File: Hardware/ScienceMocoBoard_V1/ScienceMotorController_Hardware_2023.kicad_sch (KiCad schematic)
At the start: 185 parts, among them J1 RJ45_LED_Shielded, J2 Conn_02x03_Counter_Clockwise, Q1 SI4156DY, Q10 SI4156DY, Q11 SI4156DY, Q12 SI4156DY, Q13 SI4156DY, Q14 SI4156DY, Q15 SI4156DY, Q16 SI4156DY, Q2 SI4156DY, Q3 SI4156DY, Q4 SI4156DY, Q5 SI4156DY, Q6 SI4156DY, Q7 SI4156DY, Q8 SI4156DY, Q9 SI4156DY, SW1 SW_Push, SW10 SW_Push, SW11 SW_DPDT_x2, SW2 SW_Push, SW3 SW_Push, SW4 SW_Push, SW5 SW_Push, SW6 SW_Push, SW7 SW_Push, SW8 SW_Push, SW9 SW_Push, U1 74LVC2G04, U10 IRS2005S, U11 Teensy4.1_DEV-16771, U12 74LVC2G04, U13 IRS2005S, U14 IRS2005S, U15 IRS2005S, U2 IRS2005S, U3 3V3 OKI, U4 TSR_1-2450, U5 74LVC2G04, U6 IRS2005S, U7 IRS2005S, U8 IRS2005S, U9 74LVC2G04

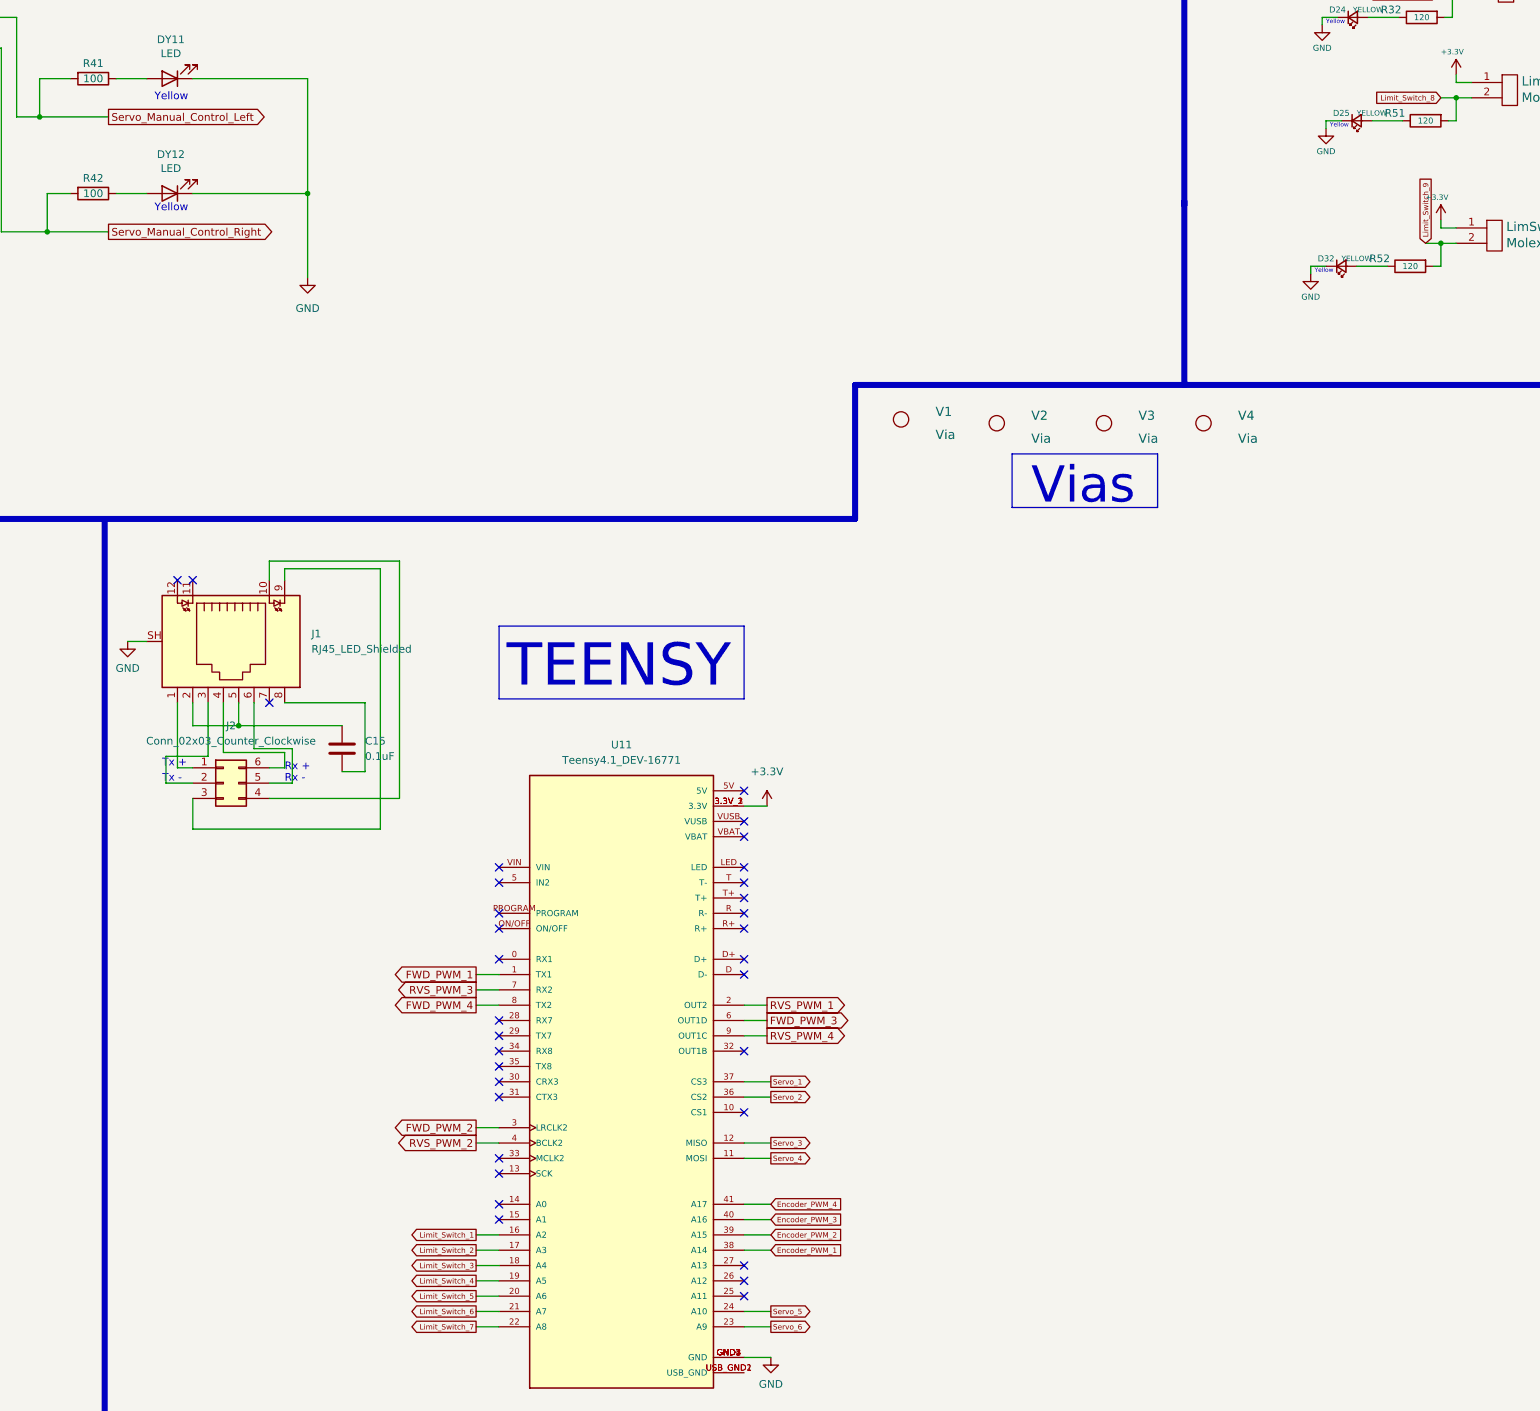
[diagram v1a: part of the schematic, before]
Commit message: H-Bridges organized and on board. PCB components sorted.
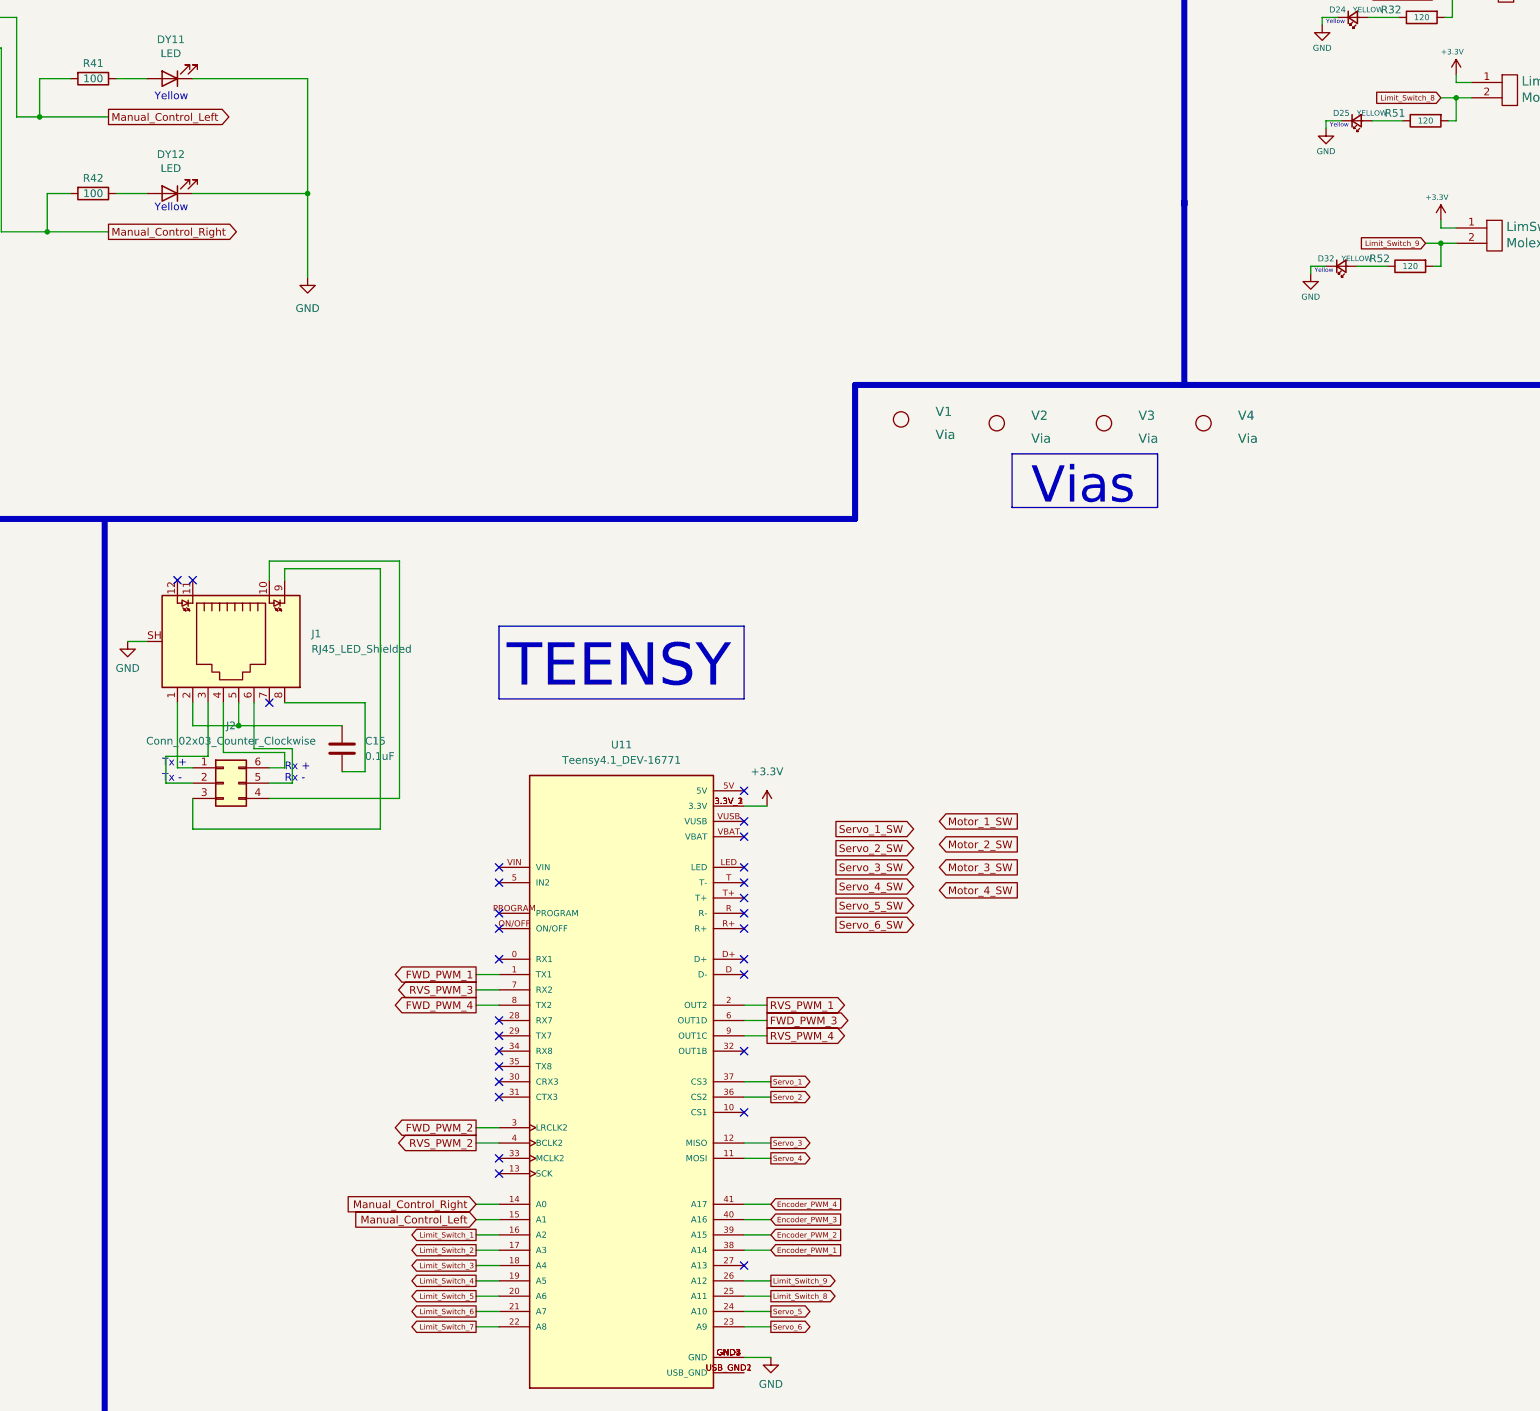
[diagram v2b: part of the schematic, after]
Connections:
- net Servo_Manual_Control_Left is gone; now on net Manual_Control_Left: R41.2, SW11.1 (A)
- net Servo_Manual_Control_Right is gone; now on net Manual_Control_Right: R42.2, SW11.3 (C)
- net Limit_Switch_8: now also U11.25 (A11)
- net Limit_Switch_9: now also U11.26 (A12)
- net Manual_Control_Right: now reaches U11.14 (A0)
- net Manual_Control_Left: now reaches U11.15 (A1)
- no-connect marks 33 -> 29
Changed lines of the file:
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@@
   (no_connect (at 422.275 319.405))
   (no_connect (at 422.275 349.885))
-  (no_connect (at 422.275 380.365))
-  (no_connect (at 422.275 377.825))
   (no_connect (at 422.275 375.285))
-  (no_connect (at 381.635 367.665))
   (no_connect (at 422.275 339.725))
   (no_connect (at 381.635 357.505))
@@
   (no_connect (at 381.635 316.865))
   (no_connect (at 381.635 319.405))
-  (no_connect (at 381.635 365.125))
   (wire (pts (xy 235.585 61.595) (xy 235.585 62.865))
     (stroke (width 0) (type default) (color 0 0 0 0))
@@
     (stroke (width 0) (type default) (color 0 0 0 0))
   )
+  (wire (pts (xy 377.825 367.665) (xy 381.635 367.665))
+    (stroke (width 0) (type default) (color 0 0 0 0))
+  )
   (wire (pts (xy 225.425 40.005) (xy 225.425 33.655))
     (stroke (width 0) (type default) (color 0 0 0 0))
@@
   )
   (wire (pts (xy 362.585 48.895) (xy 362.585 50.165))
+    (stroke (width 0) (type default) (color 0 0 0 0))
+  )
+  (wire (pts (xy 422.275 380.365) (xy 426.72 380.365))
     (stroke (width 0) (type default) (color 0 0 0 0))
   )
@@
     (stroke (width 0) (type default) (color 0 0 0 0))
   )
+  (wire (pts (xy 422.275 377.825) (xy 426.72 377.825))
+    (stroke (width 0) (type default) (color 0 0 0 0))
+  )
   (wire (pts (xy 224.79 229.87) (xy 228.6 229.87))
     (stroke (width 0) (type default) (color 0 0 0 0))
@@
   )
   (wire (pts (xy 387.985 100.965) (xy 387.985 94.615))
+    (stroke (width 0) (type default) (color 0 0 0 0))
+  )
+  (wire (pts (xy 377.825 365.125) (xy 381.635 365.125))
     (stroke (width 0) (type default) (color 0 0 0 0))
   )
@@
     )
   )
+  (global_label "Limit_Switch_8" (shape output) (at 426.72 380.365 0) (fields_autoplaced)
+    (effects (font (size 0.889 0.889)) (justify left))
+    (property "Intersheet References" "${INTERSHEET_REFS}" (id 0) (at 438.1458 380.4205 0)
+      (effects (font (size 0.889 0.889)) (justify left) hide)
+    )
+  )
   (global_label "RVS_PWM_1" (shape input) (at 264.795 40.005 0) (fields_autoplaced)
     (effects (font (size 1.27 1.27)) (justify left))
@@
     )
   )
+  (global_label "Manual_Control_Right" (shape input) (at 377.825 365.125 180) (fields_autoplaced)
+    (effects (font (size 1.27 1.27)) (justify right))
+    (property "Intersheet References" "${INTERSHEET_REFS}" (id 0) (at 354.9709 365.2044 0)
+      (effects (font (size 1.27 1.27)) (justify right) hide)
+    )
+  )
+  (global_label "Servo_2_SW" (shape output) (at 437.515 306.07 0) (fields_autoplaced)
+    (effects (font (size 1.27 1.27)) (justify left))
+    (property "Intersheet References" "${INTERSHEET_REFS}" (id 0) (at 450.9348 305.9906 0)
+      (effects (font (size 1.27 1.27)) (justify left) hide)
+    )
+  )
+  (global_label "Servo_3_SW" (shape output) (at 437.515 309.245 0) (fields_autoplaced)
+    (effects (font (size 1.27 1.27)) (justify left))
+    (property "Intersheet References" "${INTERSHEET_REFS}" (id 0) (at 450.9348 309.1656 0)
+      (effects (font (size 1.27 1.27)) (justify left) hide)
+    )
+  )
   (global_label "Motor_4_SW" (shape output) (at 233.68 219.71 0) (fields_autoplaced)
     (effects (font (size 1.27 1.27)) (justify left))
@@
     )
   )
-  (global_label "Limit_Switch_9" (shape input) (at 535.305 205.74 90) (fields_autoplaced)
-    (effects (font (size 0.889 0.889)) (justify left))
-    (property "Intersheet References" "${INTERSHEET_REFS}" (id 0) (at 535.3605 194.3142 90)
-      (effects (font (size 0.889 0.889)) (justify left) hide)
+  (global_label "Servo_5_SW" (shape output) (at 437.515 315.595 0) (fields_autoplaced)
+    (effects (font (size 1.27 1.27)) (justify left))
+    (property "Intersheet References" "${INTERSHEET_REFS}" (id 0) (at 450.9348 315.5156 0)
+      (effects (font (size 1.27 1.27)) (justify left) hide)
+    )
+  )
+  (global_label "Manual_Control_Left" (shape input) (at 377.825 367.665 180) (fields_autoplaced)
+    (effects (font (size 1.27 1.27)) (justify right))
+    (property "Intersheet References" "${INTERSHEET_REFS}" (id 0) (at 356.3014 367.7444 0)
+      (effects (font (size 1.27 1.27)) (justify right) hide)
+    )
+  )
+  (global_label "Motor_1_SW" (shape input) (at 454.66 301.625 0) (fields_autoplaced)
+    (effects (font (size 1.27 1.27)) (justify left))
+    (property "Intersheet References" "${INTERSHEET_REFS}" (id 0) (at 468.1402 301.5456 0)
+      (effects (font (size 1.27 1.27)) (justify left) hide)
+    )
+  )
+  (global_label "Limit_Switch_9" (shape input) (at 535.305 205.74 180) (fields_autoplaced)
+    (effects (font (size 0.889 0.889)) (justify right))
+    (property "Intersheet References" "${INTERSHEET_REFS}" (id 0) (at 523.8792 205.6845 0)
+      (effects (font (size 0.889 0.889)) (justify right) hide)
     )
   )
@@
     )
   )
-  (global_label "Servo_Manual_Control_Right" (shape output) (at 316.865 203.835 0) (fields_autoplaced)
-    (effects (font (size 1.27 1.27)) (justify left))
-    (property "Intersheet References" "${INTERSHEET_REFS}" (id 0) (at 345.8876 203.7556 0)
+  (global_label "Manual_Control_Right" (shape output) (at 316.865 203.835 0) (fields_autoplaced)
+    (effects (font (size 1.27 1.27)) (justify left))
+    (property "Intersheet References" "${INTERSHEET_REFS}" (id 0) (at 339.7191 203.7556 0)
       (effects (font (size 1.27 1.27)) (justify left) hide)
     )
@@
     )
   )
-  (global_label "Servo_Manual_Control_Left" (shape output) (at 316.865 184.785 0) (fields_autoplaced)
-    (effects (font (size 1.27 1.27)) (justify left))
-    (property "Intersheet References" "${INTERSHEET_REFS}" (id 0) (at 344.5571 184.7056 0)
+  (global_label "Manual_Control_Left" (shape output) (at 316.865 184.785 0) (fields_autoplaced)
+    (effects (font (size 1.27 1.27)) (justify left))
+    (property "Intersheet References" "${INTERSHEET_REFS}" (id 0) (at 338.3886 184.7056 0)
       (effects (font (size 1.27 1.27)) (justify left) hide)
     )
@@
     )
   )
+  (global_label "Servo_4_SW" (shape output) (at 437.515 312.42 0) (fields_autoplaced)
+    (effects (font (size 1.27 1.27)) (justify left))
+    (property "Intersheet References" "${INTERSHEET_REFS}" (id 0) (at 450.9348 312.3406 0)
+      (effects (font (size 1.27 1.27)) (justify left) hide)
+    )
+  )
   (global_label "RVS_PWM_2" (shape output) (at 377.825 354.965 180) (fields_autoplaced)
     (effects (font (size 1.27 1.27)) (justify right))
@@
     )
   )
+  (global_label "Servo_6_SW" (shape output) (at 437.515 318.77 0) (fields_autoplaced)
+    (effects (font (size 1.27 1.27)) (justify left))
+    (property "Intersheet References" "${INTERSHEET_REFS}" (id 0) (at 450.9348 318.6906 0)
+      (effects (font (size 1.27 1.27)) (justify left) hide)
+    )
+  )
   (global_label "Limit_Switch_8" (shape input) (at 537.845 181.61 180) (fields_autoplaced)
     (effects (font (size 0.889 0.889)) (justify right))
@@
     )
   )
+  (global_label "Motor_2_SW" (shape input) (at 454.66 305.435 0) (fields_autoplaced)
+    (effects (font (size 1.27 1.27)) (justify left))
+    (property "Intersheet References" "${INTERSHEET_REFS}" (id 0) (at 468.1402 305.3556 0)
+      (effects (font (size 1.27 1.27)) (justify left) hide)
+    )
+  )
   (global_label "RVS_PWM_4" (shape output) (at 426.085 337.185 0) (fields_autoplaced)
     (effects (font (size 1.27 1.27)) (justify left))
     (property "Intersheet References" "${INTERSHEET_REFS}" (id 0) (at 439.3838 337.1056 0)
+      (effects (font (size 1.27 1.27)) (justify left) hide)
+    )
+  )
+  (global_label "Motor_3_SW" (shape input) (at 454.66 309.245 0) (fields_autoplaced)
+    (effects (font (size 1.27 1.27)) (justify left))
+    (property "Intersheet References" "${INTERSHEET_REFS}" (id 0) (at 468.1402 309.1656 0)
       (effects (font (size 1.27 1.27)) (justify left) hide)
     )
@@
     )
   )
+  (global_label "Limit_Switch_9" (shape output) (at 426.72 377.825 0) (fields_autoplaced)
+    (effects (font (size 0.889 0.889)) (justify left))
+    (property "Intersheet References" "${INTERSHEET_REFS}" (id 0) (at 438.1458 377.8805 0)
+      (effects (font (size 0.889 0.889)) (justify left) hide)
+    )
+  )
+  (global_label "Servo_1_SW" (shape output) (at 437.515 302.895 0) (fields_autoplaced)
+    (effects (font (size 1.27 1.27)) (justify left))
+    (property "Intersheet References" "${INTERSHEET_REFS}" (id 0) (at 450.9348 302.8156 0)
+      (effects (font (size 1.27 1.27)) (justify left) hide)
+    )
+  )
   (global_label "Limit_Switch_4" (shape output) (at 377.825 377.825 180) (fields_autoplaced)
     (effects (font (size 0.889 0.889)) (justify right))
@@
     )
   )
+  (global_label "Motor_4_SW" (shape input) (at 454.66 313.055 0) (fields_autoplaced)
+    (effects (font (size 1.27 1.27)) (justify left))
+    (property "Intersheet References" "${INTERSHEET_REFS}" (id 0) (at 468.1402 312.9756 0)
+      (effects (font (size 1.27 1.27)) (justify left) hide)
+    )
+  )

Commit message: Fixed schematic
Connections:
- net +3V3: no longer AbsEncode1.1, AbsEncode2.1, AbsEncode3.1, AbsEncode4.1
- net +5V: now also AbsEncode1.2, AbsEncode2.2, AbsEncode3.2, AbsEncode4.2, R10.1; no longer R10.2
- net Encoder_PWM_1: now also AbsEncode1.1, U11.14 (A0); no longer AbsEncode1.3, U11.38 (A14)
- net Encoder_PWM_2: now also AbsEncode4.1, U11.15 (A1); no longer AbsEncode4.3, U11.39 (A15)
- net Encoder_PWM_3: now also AbsEncode2.1, U11.18 (A4); no longer AbsEncode2.3, U11.40 (A16)
- net Encoder_PWM_4: now also AbsEncode3.1, U11.19 (A5); no longer AbsEncode3.3, U11.41 (A17)
- net FWD_PWM_1: now also U11.0 (RX1); no longer U11.1 (TX1)
- net FWD_PWM_2: now also U11.2 (OUT2); no longer U11.3 (LRCLK2)
- net FWD_PWM_3: now also U11.4 (BCLK2); no longer U11.6 (OUT1D)
- net FWD_PWM_4: now also U11.6 (OUT1D); no longer U11.8 (TX2)
- net GND: now also AbsEncode1.3, AbsEncode2.3, AbsEncode3.3, AbsEncode4.3, U11.USB_GND1 (USB_GND), U11.USB_GND2 (USB_GND); no longer AbsEncode1.2, AbsEncode2.2, AbsEncode3.2, AbsEncode4.2
- net Limit_Switch_1: now also U11.23 (A9); no longer U11.16 (A2)
- net Limit_Switch_2: now also U11.22 (A8); no longer U11.17 (A3)
- net Limit_Switch_3: now also U11.21 (A7); no longer U11.18 (A4)
- net Limit_Switch_4: now also U11.20 (A6); no longer U11.19 (A5)
- net Limit_Switch_5: now also U11.17 (A3); no longer U11.20 (A6)
- net Limit_Switch_6: now also U11.16 (A2); no longer U11.21 (A7)
- net Limit_Switch_7: now also U11.41 (A17); no longer U11.22 (A8)
- net Limit_Switch_8: now also U11.40 (A16); no longer U11.25 (A11)
- net Limit_Switch_9: now also U11.39 (A15); no longer U11.26 (A12)
- net Manual_Control_Left: now also U11.37 (CS3); no longer U11.15 (A1)
- net Manual_Control_Right: now also U11.38 (A14); no longer U11.14 (A0)
- net Motor_1_SW: now also U11.27 (A13)
- net Motor_2_SW: now also U11.26 (A12)
- net Motor_3_SW: now also U11.25 (A11)
- net Motor_4_SW: now also U11.24 (A10)
- net RVS_PWM_1: now also U11.1 (TX1); no longer U11.2 (OUT2)
- net RVS_PWM_2: now also U11.3 (LRCLK2); no longer U11.4 (BCLK2)
- net RVS_PWM_3: now also U11.5 (IN2); no longer U11.7 (RX2)
- net RVS_PWM_4: now also U11.7 (RX2); no longer U11.9 (OUT1C)
- net Servo_1: now also U11.8 (TX2); no longer U11.37 (CS3)
- net Servo_1_SW: now also U11.36 (CS2)
- net Servo_2: now also U11.9 (OUT1C); no longer U11.36 (CS2)
- net Servo_2_SW: now also U11.35 (TX8)
- net Servo_3: now also U11.10 (CS1); no longer U11.12 (MISO)
- net Servo_3_SW: now also U11.34 (RX8)
- net Servo_4_SW: now also U11.33 (MCLK2)
- net Servo_5: now also U11.12 (MISO); no longer U11.24 (A10)
- net Servo_5_SW: now also U11.30 (CRX3)
- net Servo_6: now also U11.13 (SCK); no longer U11.23 (A9)
- net Servo_6_SW: now also U11.31 (CTX3)
- net at D9.2 (A): now also R10.2; no longer R10.1
- no-connect marks 29 -> 19
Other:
- note removed: "Green"
- moved on the sheet: D10, D11, D12, D13, D8, D9, R10, R16, R17, R18, R19

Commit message: Fixed encoder connections
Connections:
- net +5V: now also AbsEncode1.1, AbsEncode2.1, AbsEncode3.1, AbsEncode4.1; no longer AbsEncode1.2, AbsEncode2.2, AbsEncode3.2, AbsEncode4.2
- net Encoder_PWM_1: now also AbsEncode1.2, R17.1; no longer AbsEncode1.1, R17.2
- net Encoder_PWM_2: now also AbsEncode4.2, R16.1; no longer AbsEncode4.1, R16.2
- net Encoder_PWM_3: now also AbsEncode2.2, R18.1; no longer AbsEncode2.1, R18.2
- net Encoder_PWM_4: now also AbsEncode3.2, R19.1; no longer AbsEncode3.1, R19.2
- net at D13.2 (A): now also R19.2; no longer R19.1
- net at D11.2 (A): now also R17.2; no longer R17.1
- net at D12.2 (A): now also R18.2; no longer R18.1
- net at D10.2 (A): now also R16.2; no longer R16.1
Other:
- moved on the sheet: AbsEncode4, C15, D10, D11, D12, D13, J1, J2, R16, R17, R18, R19
